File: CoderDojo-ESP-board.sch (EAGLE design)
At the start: 50 parts, among them IC1 ESP-12E/F, IC2 FT232RL, IC3 L293D, U1 PCA9685PW,118, U2 AMS1117-3.3, X1 PN61729-S

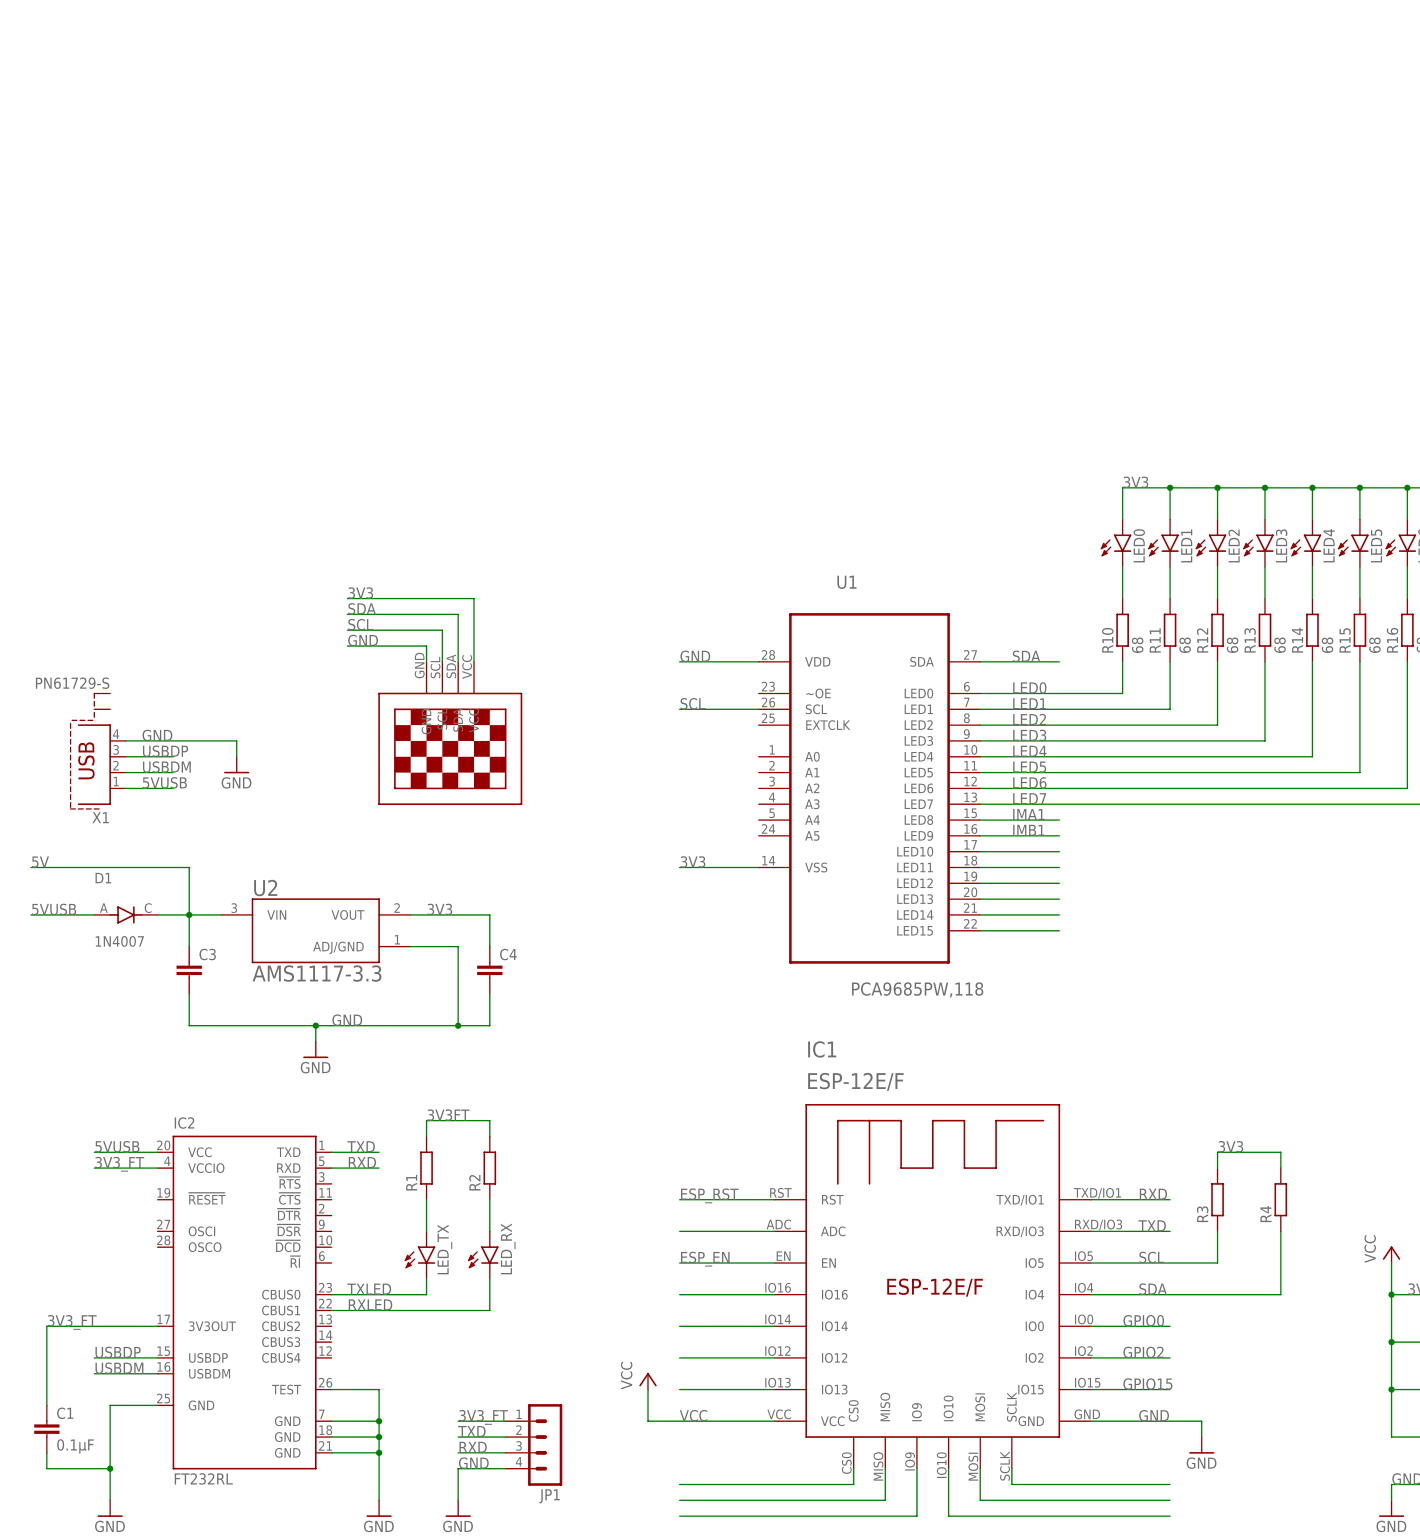
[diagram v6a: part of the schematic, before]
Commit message: Add MCP23017-E/SO package library + update Vdd Vss with correct 3v3/GND
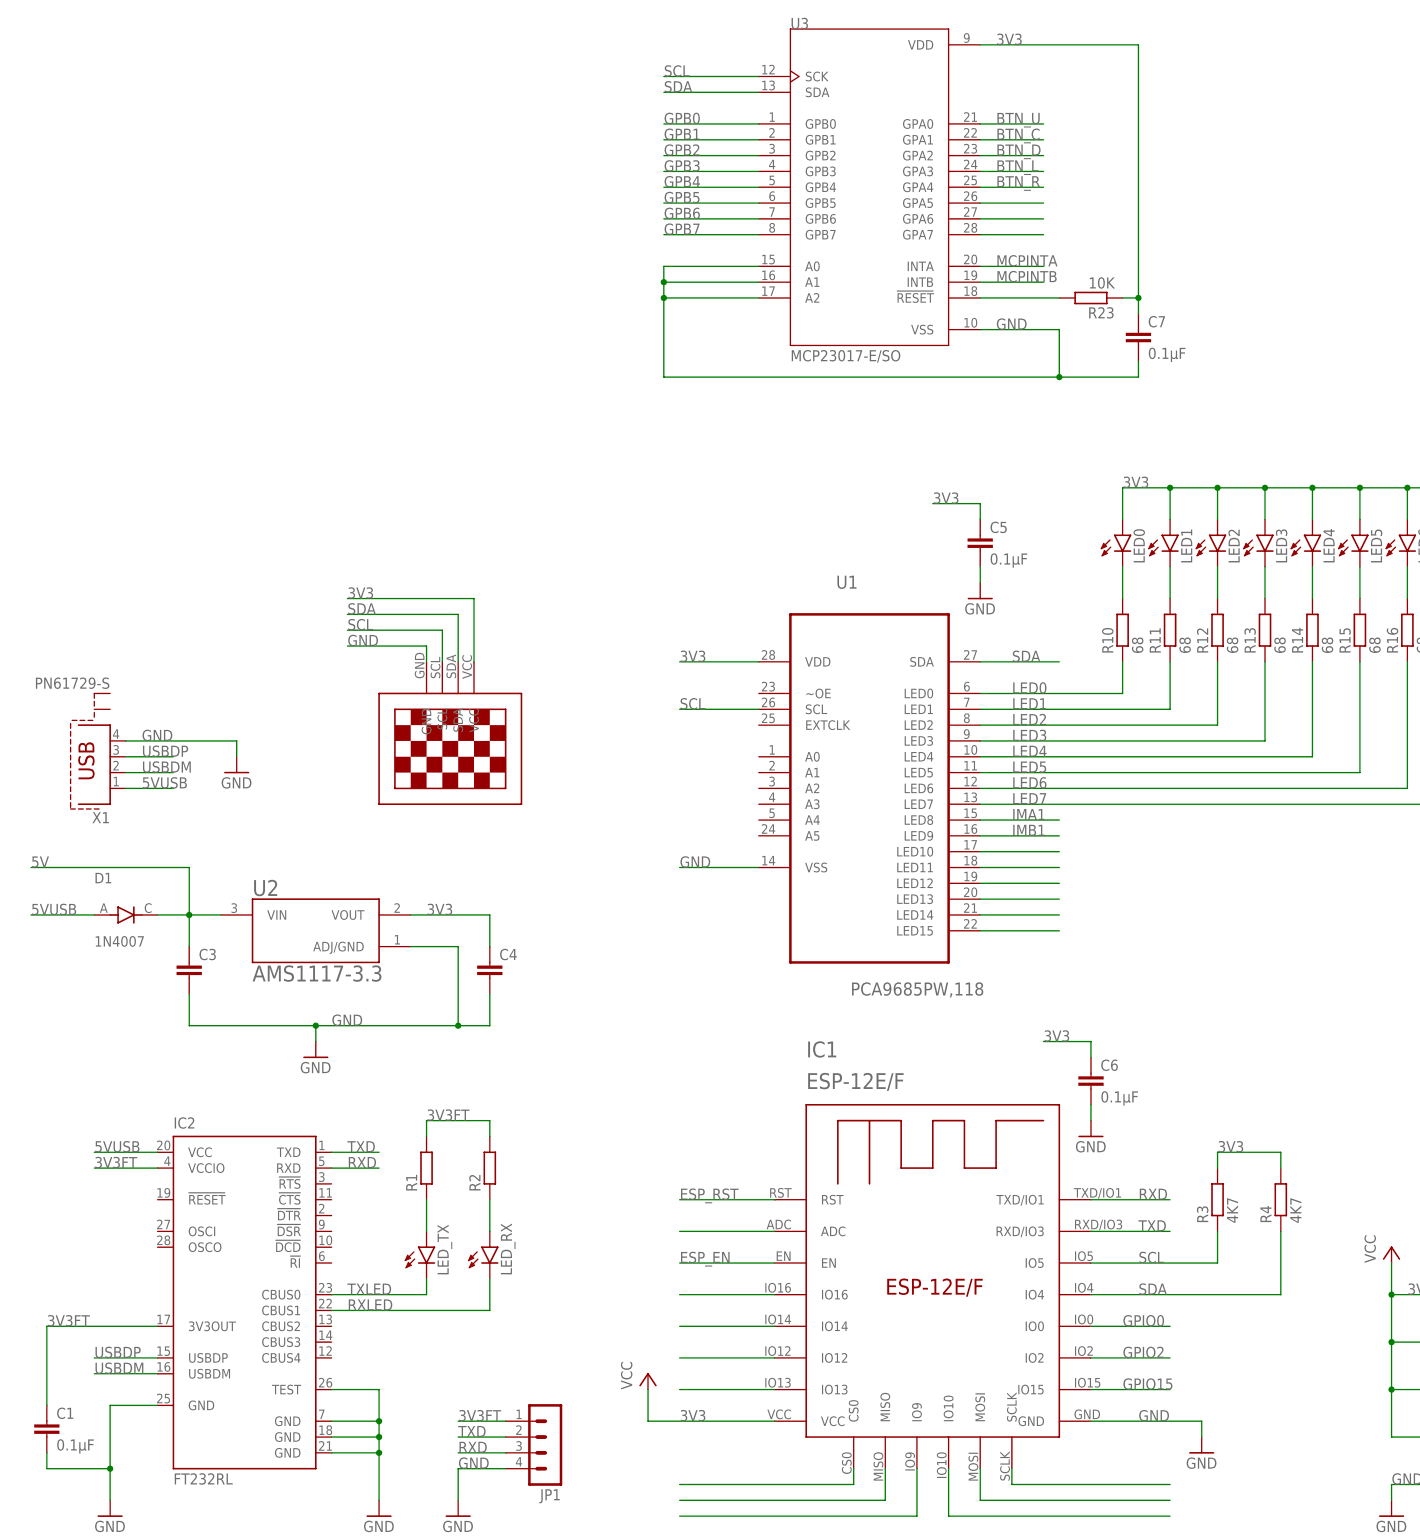
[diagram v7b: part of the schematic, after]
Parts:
- added C5, C6, C7: 0.1µF, rcl:C-EUC0805
- added R23: 10K, rcl:R-EU_R0805
- added U3: MCP23017-E/SO, MCP23017-E_SO:MCP23017-E/SO
- R3, R4: value (none) -> 4K7
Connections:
- removed net 3V3_FT: C1.1, IC2.3V3OUT, IC2.VCCIO, JP1.1
- removed net VCC: IC1.VCC
- new net GPB0: U3.GPB0
- new net GPB1: U3.GPB1
- new net GPB2: U3.GPB2
- new net GPB3: U3.GPB3
- new net GPB4: U3.GPB4
- new net GPB5: U3.GPB5
- new net GPB6: U3.GPB6
- new net GPB7: U3.GPB7
- new net MCPINTA: U3.INTA
- new net MCPINTB: U3.INTB
- new net N$10: R23.2, U3.!RESET
- new net N$15: U3.GPA6
- new net N$16: U3.GPA7
- new net N$8: U3.GPA5
- net 3V3: now also C5.1, C6.1, C7.1, IC1.VCC, R23.1, U1.VDD, U3.VDD; no longer U1.VSS
- net 3V3FT: now also C1.1, IC2.3V3OUT, IC2.VCCIO, JP1.1
- net BTN_C: now also U3.GPA1
- net BTN_D: now also U3.GPA2
- net BTN_L: now also U3.GPA3
- net BTN_R: now also U3.GPA4
- net BTN_U: now also U3.GPA0
- net GND: now also C5.2, C6.2, C7.2, U1.VSS, U3.A0, U3.A1, U3.A2, U3.VSS; no longer U1.VDD
- net SCL: now also U3.SCK
- net SDA: now also U3.SDA

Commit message: add BC817 transistor datasheet + update schematic
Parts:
- removed JP1: (no value), con-lstb:MA04-1
- removed S1, S2, S3, S4, S5: (no value), switch-omron:10-XX
- added C, D, FLASH, L, R, RESET, U: (no value), switch-omron:10-XX
- added C8: 0.1µF, rcl:C-EUC0805
- added C9: 10µF, rcl:CPOL-EUE2-5
- added JP2: (no value), con-lstb:MA04-1
- added LED_BLUE: (no value), led:LEDSML0805
- added R24, R25, R26, R27, R28, R29, R30, R31, R32, R33: 10K, rcl:R-EU_R0805
- added R34, R35: 12K, rcl:R-EU_R0805
- added R36, R37, R38, R39: 470, rcl:R-EU_R0805
- added R40: 220K, rcl:R-EU_R0805
- added R41: 100K, rcl:R-EU_R0805
- added SV1: (no value), con-lsta:FE20-2
- added SV2, SV3, SV4: (no value), con-lstb:MA03-1
- added SV5: (no value), con-lstb:MA06-1
- added T1, T2: (no value), transistor:BC817-40-NPN-SOT23-BEC
- C4: value (none) -> 10µF; device rcl:C-EUC0805 -> rcl:CPOL-EUE2-5
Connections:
- net N$6 renamed GPIO12
- removed net N$11: IC1.MOSI
- removed net N$12: IC1.IO10
- removed net N$13: IC1.MISO
- removed net N$14: IC1.CS0
- removed net N$3: IC1.SCLK
- removed net N$4: IC1.IO16
- removed net N$5: IC1.IO14
- removed net N$7: IC1.IO13
- removed net N$9: IC1.IO9
- new net ADC_EX: R40.2, SV1.25
- new net CS0: IC1.CS0, SV1.39
- new net DTR: IC2.!DTR, R34.2, SV5.6, T2.E
- new net GPA7: SV1.17, U3.GPA7
- new net GPIO10: IC1.IO10, SV1.36
- new net GPIO13: IC1.IO13, SV1.31
- new net GPIO14: IC1.IO14, SV1.32
- new net GPIO16: IC1.IO16, LED_BLUE.C, R39.2, SV1.30
- new net GPIO9: IC1.IO9, SV1.35
- new net MISO: IC1.MISO, SV1.37
- new net MOSI: IC1.MOSI, SV1.38
- new net N$18: R26.2, U3.A1
- new net N$19: R27.2, U3.A0
- new net N$20: R29.2, U1.A1
- new net N$35: R37.1, R39.1, RESET.S
- new net N$36: FLASH.S, R36.1
- new net N$37: LED_BLUE.A, R38.1
- new net PWM10: SV1.18, SV3.3, U1.LED10
- new net PWM11: SV1.19, SV2.3, U1.LED11
- new net PWM12: SV1.20, SV4.3, U1.LED12
- new net PWM13: SV1.21, U1.LED13
- new net PWM14: SV1.22, U1.LED14
- new net PWM15: SV1.23, U1.LED15
- new net RTS: IC2.!RTS, R35.2, SV5.5, T1.E
- new net SCLK: IC1.SCLK, SV1.40
- net 3V3: now also C.S, C5.2, C6.2, C9.+, D.S, L.S, R.S, R38.2, SV1.4, U.S; no longer C4.1, C5.1, C6.1, S1.S, S2.S, S3.S, S4.S, S5.S
- net 3V3FT: no longer JP1.1
- net 5V: now also SV1.6, SV2.2, SV3.2, SV4.2, SV5.1
- net 5VUSB: now also C8.1
- net BTN_C: now also C.P; no longer S2.P
- net BTN_D: now also D.P; no longer S3.P
- net BTN_L: now also L.P; no longer S4.P
- net BTN_R: now also R.P; no longer S5.P
- net BTN_U: now also U.P; no longer S1.P
- net ESP_EN: now also SV1.28
- net ESP_RST: now also R37.2, SV1.27, T1.C
- net GND: now also C2.2, C4.-, C5.1, C6.1, C8.2, C9.-, FLASH.P, R24.1, R25.1, R26.1, R27.1, R28.1, R29.1, R30.1, R31.1, R32.1, R33.1, R41.1, RESET.P, SV1.2, SV1.5, SV2.1, SV3.1, SV4.1, SV5.2; no longer C4.2, C5.2, C6.2, JP1.4, U3.A0, U3.A1, U3.A2
- net GPB0: now also SV1.9
- net GPB1: now also SV1.10
- net GPB2: now also SV1.11
- net GPB3: now also SV1.12
- net GPB4: now also SV1.13
- net GPB5: now also SV1.14
- net GPB6: now also SV1.15
- net GPB7: now also SV1.16
- net GPIO0: now also R36.2, SV1.33, T2.C
- net GPIO15: now also SV1.29
- net GPIO2: now also SV1.34
- net IMA2: now also U3.GPA5
- net IMB2: now also U3.GPA6
- net N$15: now also R28.2, U1.A0; no longer U3.GPA6
- net N$16: now also R25.2, U3.A2; no longer U3.GPA7
- net N$17: now also R40.1, R41.2
- net N$21: now also R30.2, U1.A2; no longer U1.LED10
- net N$22: now also R31.2, U1.A3; no longer U1.LED11
- net N$23: now also R32.2, U1.A4; no longer U1.LED12
- net N$24: now also R33.2, U1.A5; no longer U1.LED13
- net N$25: now also R34.1, T1.B; no longer U1.LED14
- net N$26: now also R35.1, T2.B; no longer U1.LED15
- net N$8: now also R24.2, U1.~OE; no longer U3.GPA5
- net OMA1: now also JP2.1
- net OMA2: now also JP2.2
- net OMB1: now also JP2.3
- net OMB2: now also JP2.4
- net RXD: now also SV1.26, SV5.4; no longer JP1.3
- net SCL: now also SV1.3
- net SDA: now also SV1.1
- net TXD: now also SV1.24, SV5.3; no longer JP1.2
- net VCC_MOTOR: now also C4.+, SV1.7, SV1.8
